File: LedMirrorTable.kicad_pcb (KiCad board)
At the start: 2 copper layers, 25.9 x 17.8 mm, 7 parts, among them IC101 ATMEGA328P-A, J101 POWER_JACKSMD, P101 CONN_01X03

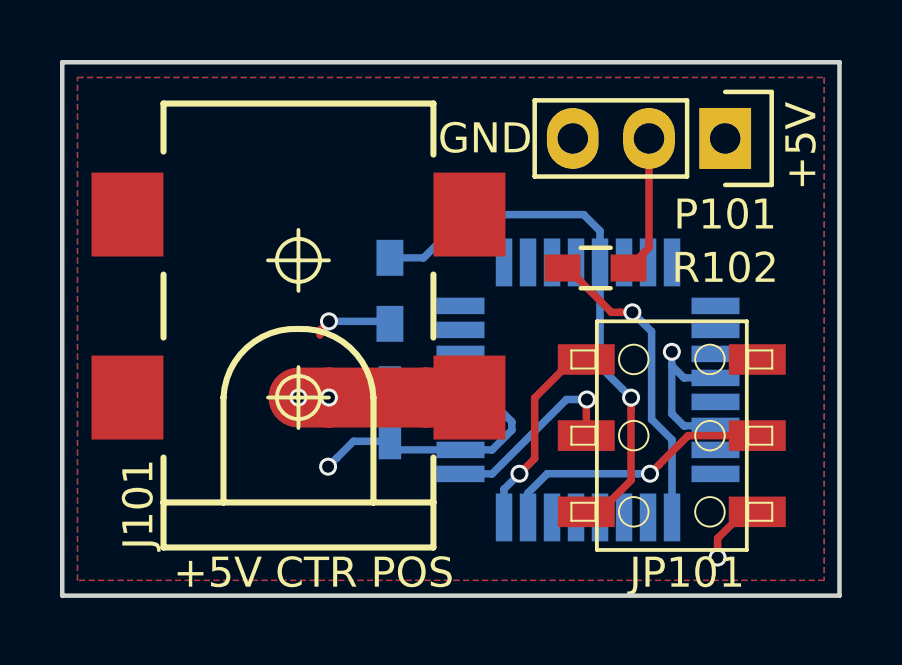
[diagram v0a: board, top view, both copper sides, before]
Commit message: Fixed a few cosmetic errors
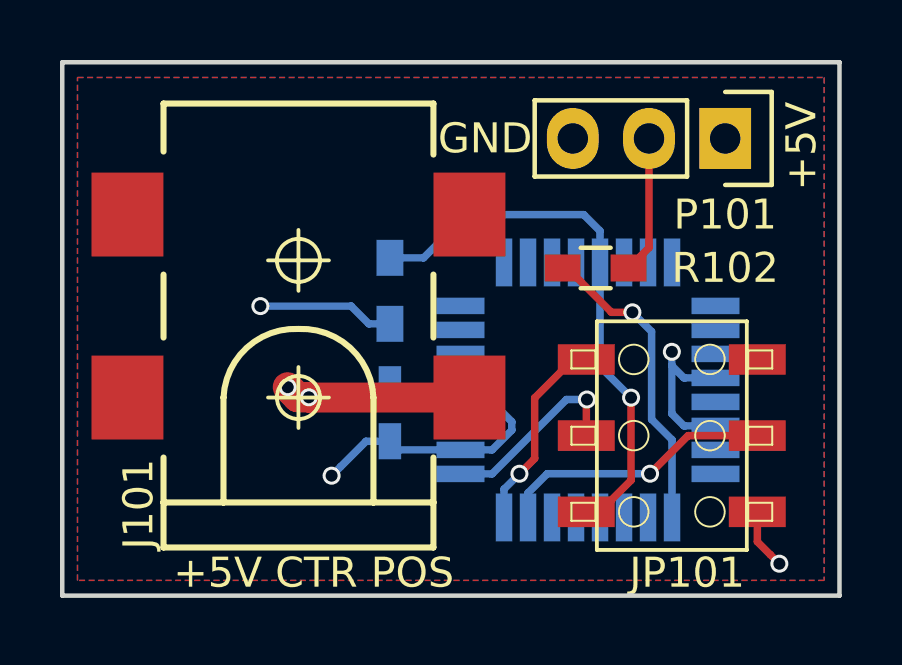
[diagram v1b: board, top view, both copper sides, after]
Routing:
- net +5V: track 17.1 -> 19.0 mm
- net GND: track 8.22 -> 8.92 mm
